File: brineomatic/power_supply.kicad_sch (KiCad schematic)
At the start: 31 parts, among them J10 5.08MM, J9 5.08MM, Q3 20N06, U2 LM74700, U3 XL1509-5.0, U4 MAX40200AUK

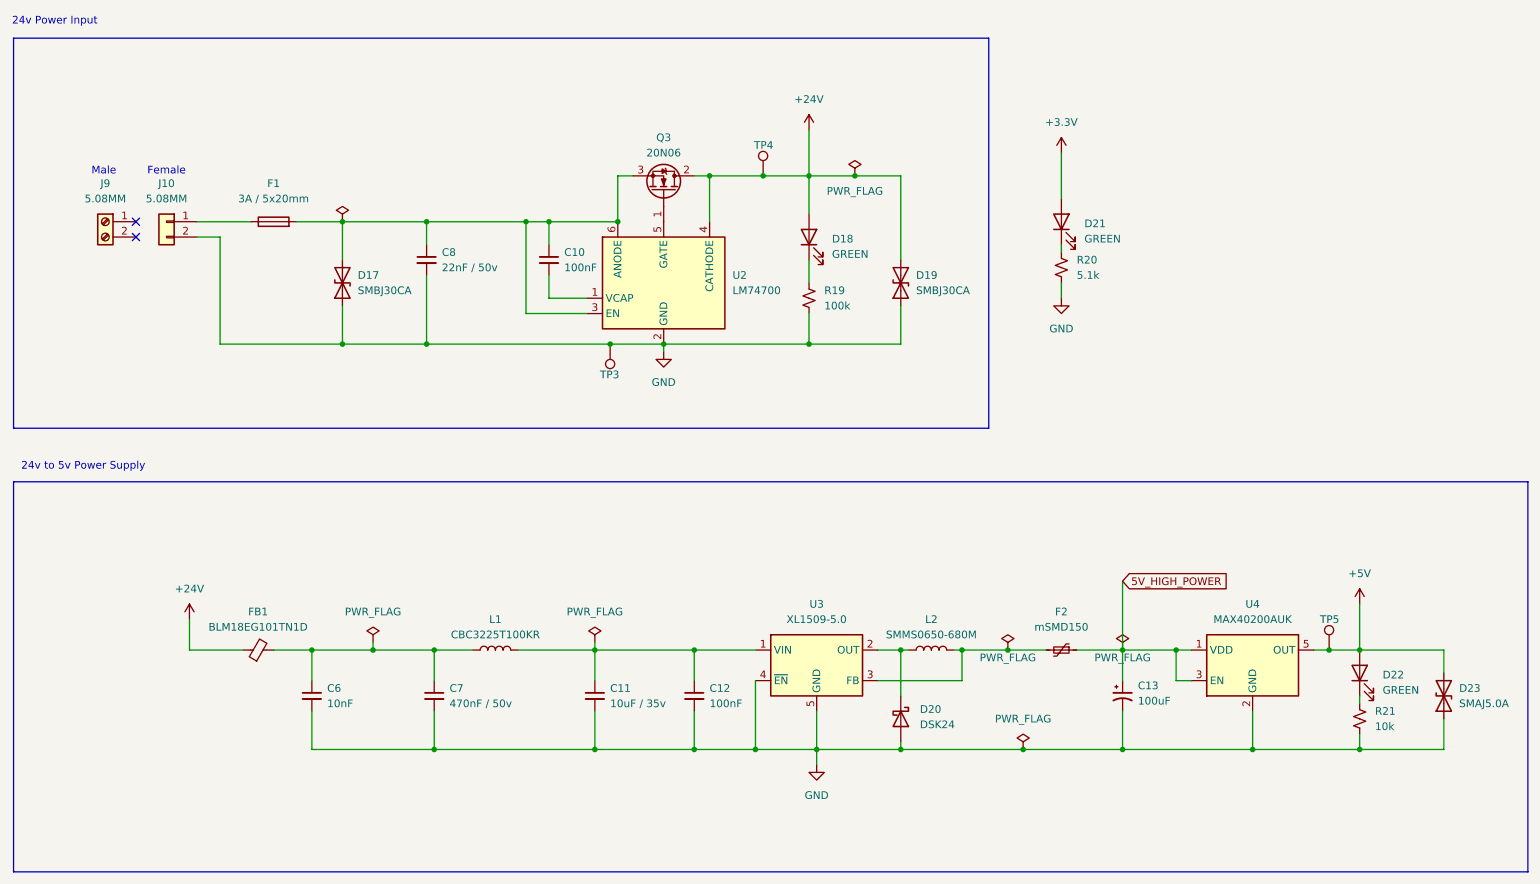
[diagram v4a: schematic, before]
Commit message: switched to the LDL1117 ldo
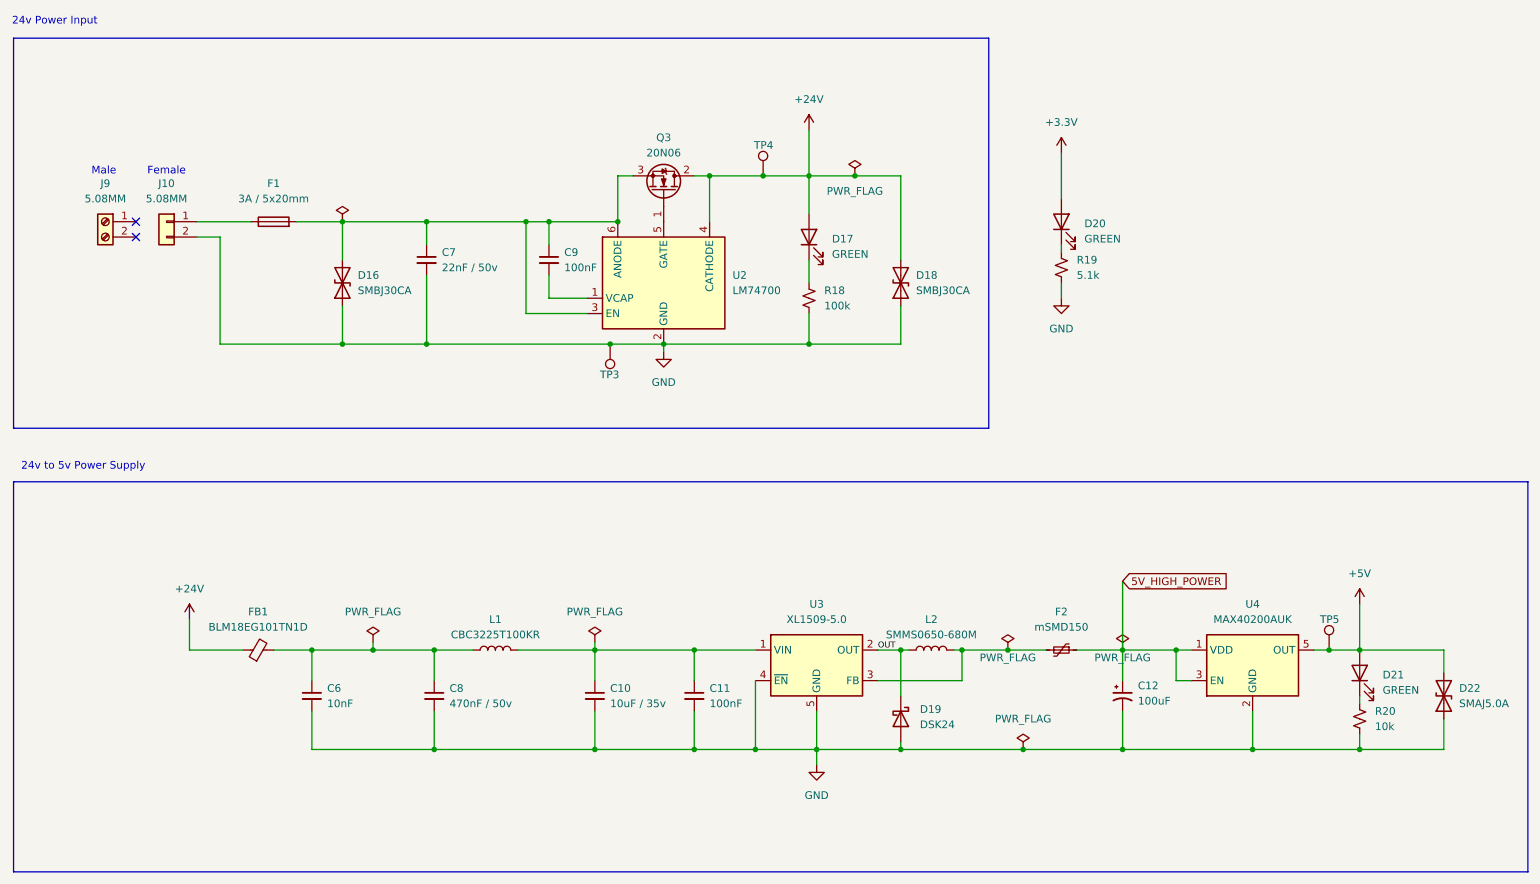
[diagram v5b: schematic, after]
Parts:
- renumbered C11 to C10, C12 to C11, C13 to C12, C8 to C7, C7 to C8, C10 to C9, D17 to D16, D18 to D17, D19 to D18, D20 to D19, D21 to D20, D22 to D21, D23 to D22, R19 to R18, R20 to R19, R21 to R20
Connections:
- net OUT: now reaches D19.1 (K), L2.1, U3.2 (OUT)
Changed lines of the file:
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@@
 		)
 	)
+	(label "OUT"
+		(at 165.1 123.19 0)
+		(effects
+			(font
+				(size 1 1)
+			)
+			(justify left bottom)
+		)
+	)
 	(global_label "5V_HIGH_POWER"
 		(shape input)
@@
 		(dnp no)
 		(fields_autoplaced yes)
-		(property "Reference" "#FLG01"
+		(property "Reference" "#FLG02"
 			(at 81.28 120.015 0)
 			(effects
@@
 			(project "brineomatic"
 				(path "/96477ae2-ef08-48f3-8dd4-fe4478541f68/7cbb3b3c-cf93-4880-b816-c6df902b993c"
-					(reference "#FLG01")
+					(reference "#FLG02")
 					(unit 1)
 				)
@@
 		(dnp no)
 		(fields_autoplaced yes)
-		(property "Reference" "D20"
+		(property "Reference" "D19"
 			(at 172.085 133.0325 90)
 			(effects
@@
 			(project "brineomatic"
 				(path "/96477ae2-ef08-48f3-8dd4-fe4478541f68/7cbb3b3c-cf93-4880-b816-c6df902b993c"
-					(reference "D20")
+					(reference "D19")
 					(unit 1)
 				)
@@
 		(dnp no)
 		(fields_autoplaced yes)
-		(property "Reference" "D18"
+		(property "Reference" "D17"
 			(at 157.48 54.9274 90)
 			(effects
@@
 			(project ""
 				(path "/96477ae2-ef08-48f3-8dd4-fe4478541f68/7cbb3b3c-cf93-4880-b816-c6df902b993c"
-					(reference "D18")
+					(reference "D17")
 					(unit 1)
 				)
@@
 		(dnp no)
 		(fields_autoplaced yes)
-		(property "Reference" "C13"
+		(property "Reference" "C12"
 			(at 208.28 129.1081 0)
 			(effects
@@
 			(project "brineomatic"
 				(path "/96477ae2-ef08-48f3-8dd4-fe4478541f68/7cbb3b3c-cf93-4880-b816-c6df902b993c"
-					(reference "C13")
+					(reference "C12")
 					(unit 1)
 				)
@@
 		(on_board yes)
 		(dnp no)
-		(property "Reference" "D19"
+		(property "Reference" "D18"
 			(at 171.45 60.96 90)
 			(effects
@@
 			(project "brineomatic"
 				(path "/96477ae2-ef08-48f3-8dd4-fe4478541f68/7cbb3b3c-cf93-4880-b816-c6df902b993c"
-					(reference "D19")
+					(reference "D18")
 					(unit 1)
 				)
@@
 		(dnp no)
 		(fields_autoplaced yes)
-		(property "Reference" "C12"
+		(property "Reference" "C11"
 			(at 137.16 129.5463 0)
 			(effects
@@
 			(project "brineomatic"
 				(path "/96477ae2-ef08-48f3-8dd4-fe4478541f68/7cbb3b3c-cf93-4880-b816-c6df902b993c"
-					(reference "C12")
+					(reference "C11")
 					(unit 1)
 				)
@@
 		(on_board yes)
 		(dnp no)
-		(property "Reference" "C8"
+		(property "Reference" "C7"
 			(at 92.71 57.1563 0)
 			(effects
@@
 			(project "brineomatic"
 				(path "/96477ae2-ef08-48f3-8dd4-fe4478541f68/7cbb3b3c-cf93-4880-b816-c6df902b993c"
-					(reference "C8")
+					(reference "C7")
 					(unit 1)
 				)
@@
 		(on_board yes)
 		(dnp no)
-		(property "Reference" "D17"
+		(property "Reference" "D16"
 			(at 78.74 60.96 90)
 			(effects
@@
 			(project "brineomatic"
 				(path "/96477ae2-ef08-48f3-8dd4-fe4478541f68/7cbb3b3c-cf93-4880-b816-c6df902b993c"
-					(reference "D17")
+					(reference "D16")
 					(unit 1)
 				)
@@
 		(dnp no)
 		(fields_autoplaced yes)
-		(property "Reference" "C10"
+		(property "Reference" "C9"
 			(at 113.03 57.1563 0)
 			(effects
@@
 			(project "brineomatic"
 				(path "/96477ae2-ef08-48f3-8dd4-fe4478541f68/7cbb3b3c-cf93-4880-b816-c6df902b993c"
-					(reference "C10")
+					(reference "C9")
 					(unit 1)
 				)
@@
 		(dnp no)
 		(fields_autoplaced yes)
-		(property "Reference" "D21"
+		(property "Reference" "D20"
 			(at 199.39 52.3874 90)
 			(effects
@@
 			(project "brineomatic"
 				(path "/96477ae2-ef08-48f3-8dd4-fe4478541f68/7cbb3b3c-cf93-4880-b816-c6df902b993c"
-					(reference "D21")
+					(reference "D20")
 					(unit 1)
 				)
@@
 		(dnp no)
 		(fields_autoplaced yes)
-		(property "Reference" "R21"
+		(property "Reference" "R20"
 			(at 247.65 133.3499 0)
 			(effects
@@
 			(project "brineomatic"
 				(path "/96477ae2-ef08-48f3-8dd4-fe4478541f68/7cbb3b3c-cf93-4880-b816-c6df902b993c"
-					(reference "R21")
+					(reference "R20")
 					(unit 1)
 				)
@@
 		(dnp no)
 		(fields_autoplaced yes)
-		(property "Reference" "R19"
+		(property "Reference" "R18"
 			(at 156.21 63.4999 0)
 			(effects
@@
 			(project ""
 				(path "/96477ae2-ef08-48f3-8dd4-fe4478541f68/7cbb3b3c-cf93-4880-b816-c6df902b993c"
-					(reference "R19")
+					(reference "R18")
 					(unit 1)
 				)
@@
 		(dnp no)
 		(fields_autoplaced yes)
-		(property "Reference" "D22"
+		(property "Reference" "D21"
 			(at 248.92 127.3174 90)
 			(effects
@@
 			(project "brineomatic"
 				(path "/96477ae2-ef08-48f3-8dd4-fe4478541f68/7cbb3b3c-cf93-4880-b816-c6df902b993c"
-					(reference "D22")
+					(reference "D21")
 					(unit 1)
 				)
@@
 		(dnp no)
 		(fields_autoplaced yes)
-		(property "Reference" "C11"
+		(property "Reference" "C10"
 			(at 120.65 129.5463 0)
 			(effects
@@
 			(project "brineomatic"
 				(path "/96477ae2-ef08-48f3-8dd4-fe4478541f68/7cbb3b3c-cf93-4880-b816-c6df902b993c"
-					(reference "C11")
+					(reference "C10")
 					(unit 1)
 				)
@@
 		(on_board yes)
 		(dnp no)
-		(property "Reference" "#FLG02"
+		(property "Reference" "#FLG01"
 			(at 76.2 50.165 0)
 			(effects
@@
 			(project "brineomatic"
 				(path "/96477ae2-ef08-48f3-8dd4-fe4478541f68/7cbb3b3c-cf93-4880-b816-c6df902b993c"
-					(reference "#FLG02")
+					(reference "#FLG01")
 					(unit 1)
 				)
@@
 		(dnp no)
 		(fields_autoplaced yes)
-		(property "Reference" "C7"
+		(property "Reference" "C8"
 			(at 93.98 129.5463 0)
 			(effects
@@
 			(project "brineomatic"
 				(path "/96477ae2-ef08-48f3-8dd4-fe4478541f68/7cbb3b3c-cf93-4880-b816-c6df902b993c"
-					(reference "C7")
+					(reference "C8")
 					(unit 1)
 				)
@@
 		(on_board yes)
 		(dnp no)
-		(property "Reference" "D23"
+		(property "Reference" "D22"
 			(at 261.62 129.54 90)
 			(effects
@@
 			(project "brineomatic"
 				(path "/96477ae2-ef08-48f3-8dd4-fe4478541f68/7cbb3b3c-cf93-4880-b816-c6df902b993c"
-					(reference "D23")
+					(reference "D22")
 					(unit 1)
 				)
@@
 		(dnp no)
 		(fields_autoplaced yes)
-		(property "Reference" "R20"
+		(property "Reference" "R19"
 			(at 198.12 58.4199 0)
 			(effects
@@
 			(project "brineomatic"
 				(path "/96477ae2-ef08-48f3-8dd4-fe4478541f68/7cbb3b3c-cf93-4880-b816-c6df902b993c"
-					(reference "R20")
+					(reference "R19")
 					(unit 1)
 				)

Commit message: switch to rt7272b for 24v -> 5v regulator
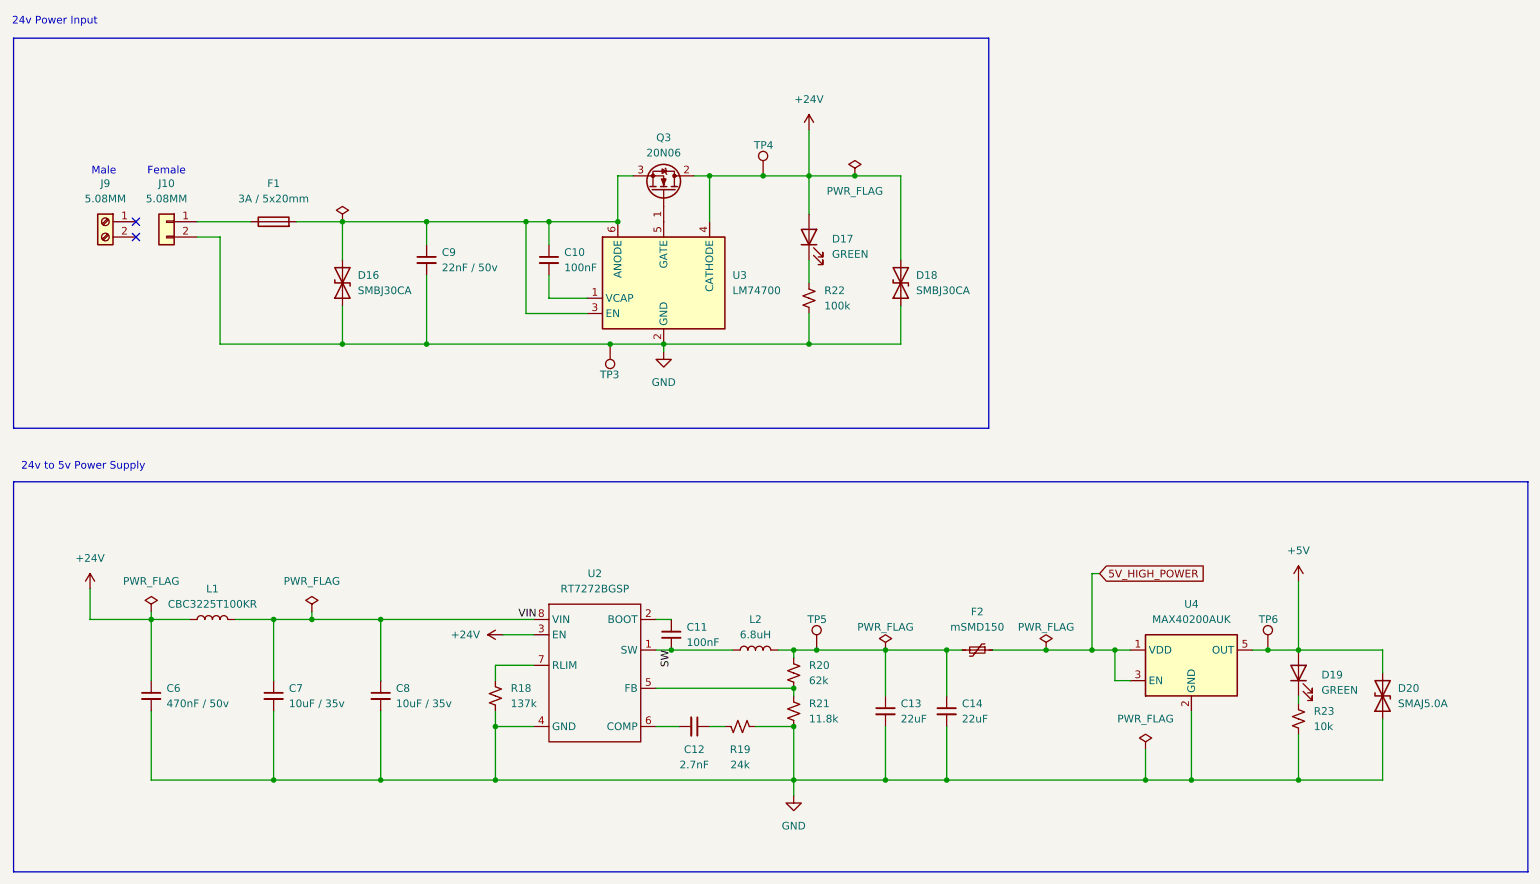
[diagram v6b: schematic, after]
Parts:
- removed C12: 100uF, Capacitor_Tantalum_SMD:CP_EIA-3528-21_Kemet-B, symbol Device:C_Polarized_Small_US
- removed C6: 10nF, Capacitor_SMD:C_0603_1608Metric, symbol Device:C_Small
- removed D19: DSK24, Diode_SMD:D_SOD-123, symbol Device:D_Schottky
- removed D20: GREEN, LED_SMD:LED_0603_1608Metric, symbol Device:LED
- removed FB1: BLM18EG101TN1D, Inductor_SMD:L_0603_1608Metric, symbol Device:FerriteBead_Small
- removed U3: XL1509-5.0, Package_SO:SOIC-8_3.9x4.9mm_P1.27mm, symbol Regulator_Switching:XL1509-5.0
- added C12: 2.7nF, Capacitor_SMD:C_0603_1608Metric, symbol Device:C_Small
- added C13, C14: 22uF, Capacitor_SMD:C_0603_1608Metric, symbol Device:C_Small
- added C8: 10uF / 35v, Capacitor_SMD:C_0805_2012Metric, symbol Device:C_Small
- added R18: 137k, Resistor_SMD:R_0603_1608Metric, symbol Device:R_Small_US
- added R20: 62k, Resistor_SMD:R_0603_1608Metric, symbol Device:R_Small_US
- added R21: 11.8k, Resistor_SMD:R_0603_1608Metric, symbol Device:R_Small_US
- added TP5: ~, TestPoint:TestPoint_THTPad_D1.5mm_Drill0.7mm, symbol Connector:TestPoint
- added U2: RT7272BGSP, yarrboard:SOIC-8_L5.0-W4.0-P1.27-LS6.0-BL-EP2.0, symbol yarrboard:RT7272B
- C7: renamed from C10; footprint Capacitor_SMD:C_1206_3216Metric_Pad1.33x1.80mm_HandSolder -> Capacitor_SMD:C_0805_2012Metric; LCSC C454102 -> (none)
- L2: value SMMS0650-680M -> 6.8uH; footprint Inductor_SMD:L_Chilisin_BMRB00060650 -> Inductor_SMD:L_Chilisin_BMRA00050530; LCSC C2894721 -> C177249; PN (none) -> SMMS0530-6R8M
- R19: value 5.1k -> 24k
- renumbered C9 to C10, C8 to C6, C7 to C9, D21 to D19, D22 to D20, R18 to R22, R20 to R23, TP5 to TP6, U2 to U3
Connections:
- net +24V: now also C6.1, L1.1, U2.3 (EN)
- net GND: now also C13.2, C14.2, C8.2, R18.2, R21.2, U2.4 (GND); no longer C11.2
- net VIN: now reaches C7.1, L1.2
- net VIN: now also C8.1, U2.8 (VIN); no longer C11.1
- net at F2.2, L2.2: now also C13.1, C14.1, R20.1, TP5.1
- net at R19.1: now also C12.1
- net OUT renamed SW
- net SW: now also C11.2, U2.1 (SW)
- new net: R20.2, R21.1, U2.5 (FB)
- new net: C11.1, U2.2 (BOOT)
- new net: C12.2, U2.6 (COMP)
- new net: R18.1, U2.7 (RLIM)
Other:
- moved on the sheet: C6, C7, D19, D20, F2, L1, L2, R23, TP6, U4

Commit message: switched back to bigger capacitors after reading datasheet
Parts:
- C13, C14: footprint Capacitor_SMD:C_0603_1608Metric -> Capacitor_SMD:C_1206_3216Metric
- C7, C8: footprint Capacitor_SMD:C_0805_2012Metric -> Capacitor_SMD:C_1210_3225Metric
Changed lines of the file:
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@@
 			)
 		)
-		(property "Footprint" "Capacitor_SMD:C_0603_1608Metric"
+		(property "Footprint" "Capacitor_SMD:C_1206_3216Metric"
 			(at 166.37 133.35 0)
 			(effects
@@
 			)
 		)
-		(property "Footprint" "Capacitor_SMD:C_0805_2012Metric"
+		(property "Footprint" "Capacitor_SMD:C_1210_3225Metric"
 			(at 82.55 130.81 0)
 			(effects
@@
 			)
 		)
-		(property "Footprint" "Capacitor_SMD:C_0603_1608Metric"
+		(property "Footprint" "Capacitor_SMD:C_1206_3216Metric"
 			(at 176.53 133.35 0)
 			(effects
@@
 			)
 		)
-		(property "Footprint" "Capacitor_SMD:C_0805_2012Metric"
+		(property "Footprint" "Capacitor_SMD:C_1210_3225Metric"
 			(at 64.77 130.81 0)
 			(effects
